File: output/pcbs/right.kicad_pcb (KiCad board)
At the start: 2 copper layers, 139.8 x 121.8 mm, 64 parts

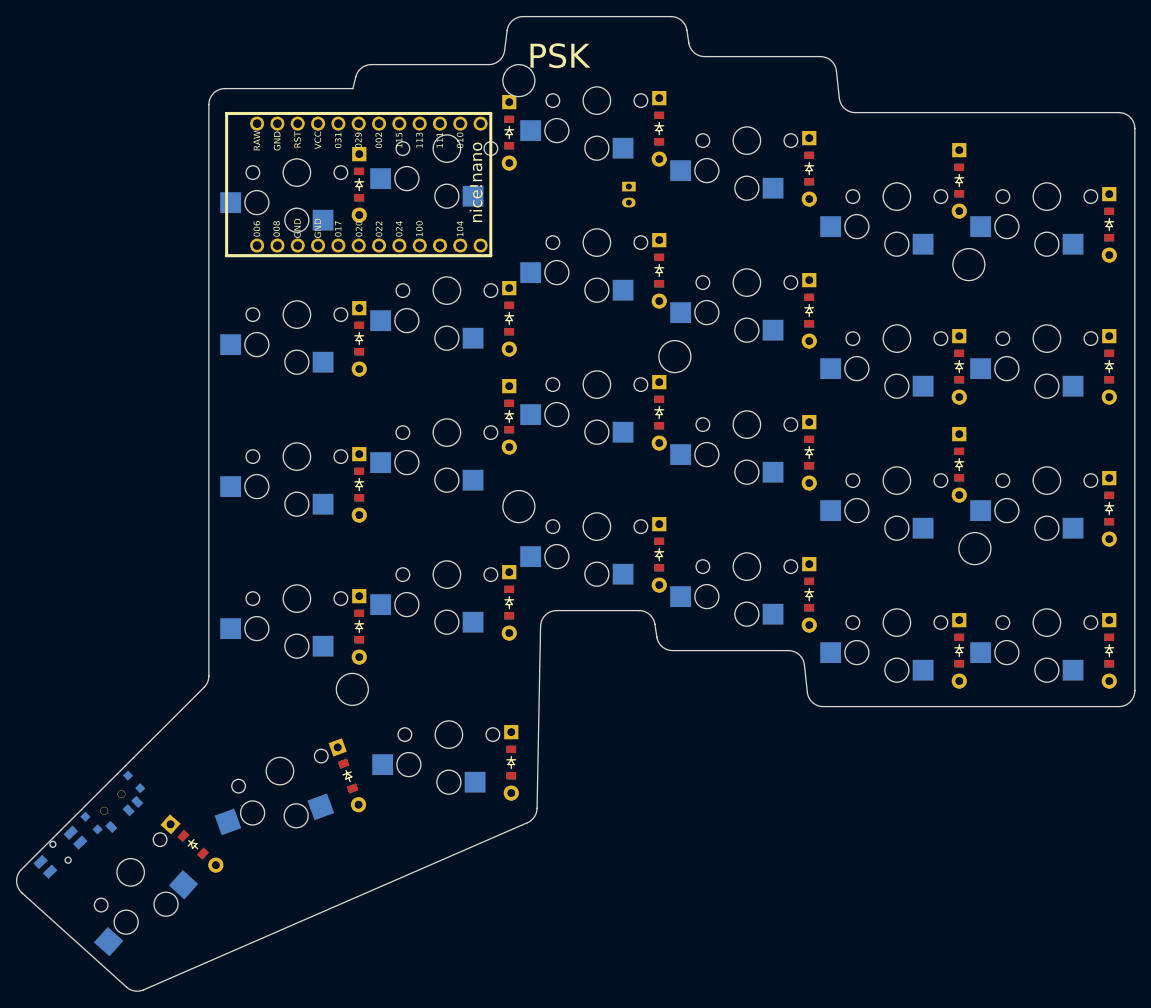
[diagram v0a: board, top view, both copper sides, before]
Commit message: Removing autosave right pcb, locks and stuff I guess
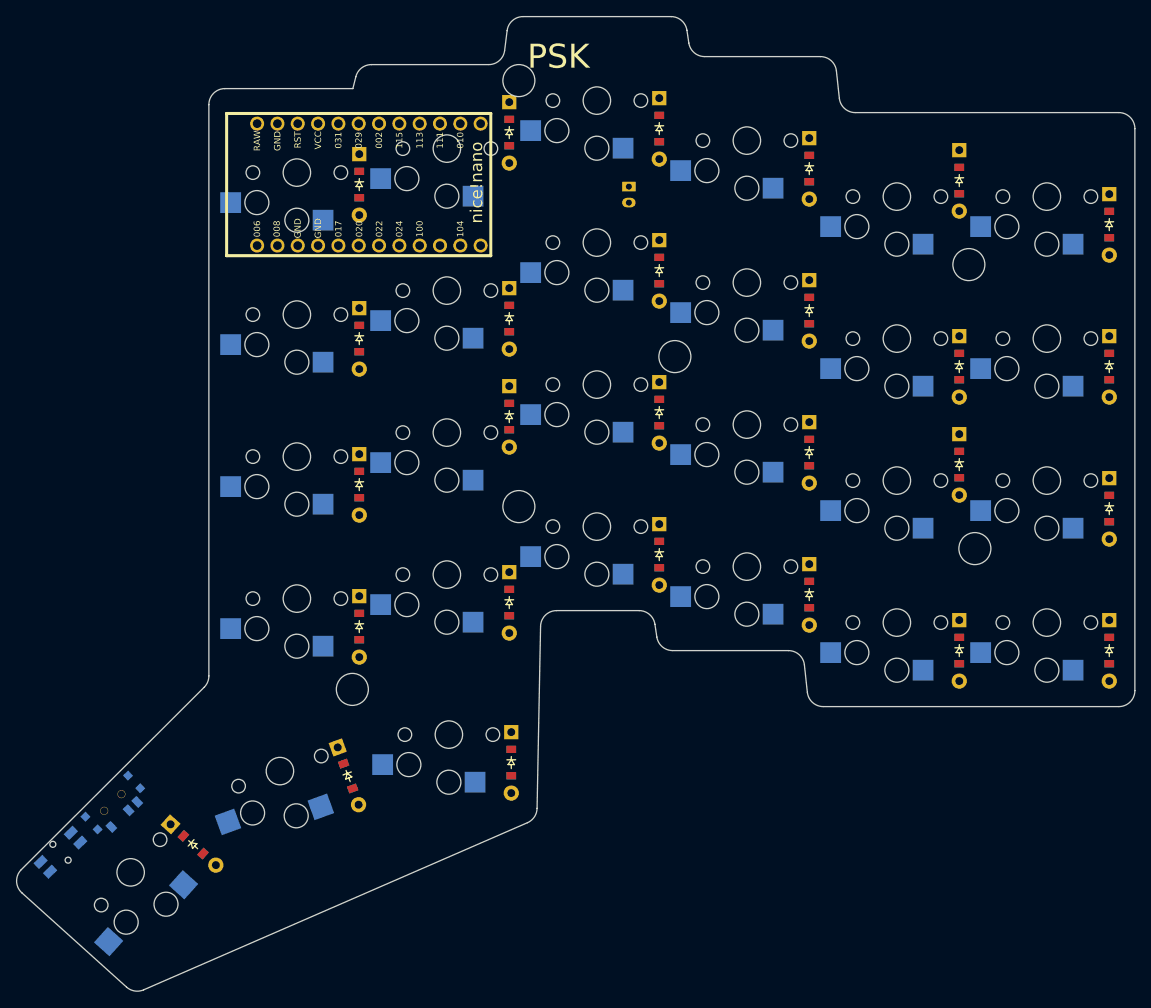
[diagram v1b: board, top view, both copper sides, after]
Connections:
- D18 pad 1: P031 -> (no net)
- D19 pad 1: P031 -> (no net)
- D20 pad 1: P031 -> (no net)
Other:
- outline, holes or cut-outs redrawn
- net class Default removed
